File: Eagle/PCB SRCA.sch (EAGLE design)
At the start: 59 parts, among them IC1 DSPIC30F4011-30I_P, IC2 LM324LVIDR, IC3 LMT86QDCKRQ1, IC4 TXB0108PWR, IC5 LORA_MOTE, J1 TBL002A-350-03GR-2OR, J2 TBL002A-350-03GR-2OR, J3 TBL002A-350-03GR-2OR, J4 172447-0004, Q1 TIP41C, T1 2N3904, T10 2N3904, T11 2N3904, T2 2N3904, T3 2N3904, T4 2N3904, T5 2N3904, T6 2N3904, T7 2N3904, T8 2N3904, T9 2N3904

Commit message: 14/07/2021
actualizacIón de la PCB
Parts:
- removed C4: C0805X104K1RAC3316, C0805X104K1RAC3316:C0805X104K1RAC3316
- removed IC5: LORA_MOTE, LORA_MOTE:LORA_MOTE
- removed R17: ERA6AEB101V, ERA6AEB101V:ERA6AEB101V
- IC4: value TXB0108PWR -> LORA_MOTE; device TXB0108PWR:TXB0108PWR -> LORA_MOTE:LORA_MOTE
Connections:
- removed net FAN2: D1.A, J2.B1, Q1.C
- removed net GND2: T11.E
- removed net N$20: IC4.OE, R17.2
- removed net V1: R18.2
- removed net V3: IC4.VCCA
- new net I2C_SCL: IC1.PGD/EMUD/U1TX/SDO1/SCL/RF3, J3.A2
- new net I2C_SDA: IC1.PGC/EMUC/U1RX/SDI1/SDA/RF2, J3.B1
- new net TX_UART2: IC1.U2TX/CN18/RF5
- net FAN1: now also D1.A, J2.B1, Q1.C; no longer D1.C, J2.A2
- net GND: no longer C4.1, IC5.GND, R17.1
- net GND1: now also T11.E
- net RX_LORA: now also IC4.UARTTX; no longer IC4.A1, IC5.UARTTX
- net RX_UART: no longer IC4.B1
- net SONAR_ADC: now also J2.A2; no longer J2.A1
- net TX_LORA: now also IC4.UARTRX; no longer IC4.A2, IC5.UARTRX
- net TX_UART: no longer IC4.B2
- net V5: now also D1.C, IC4.V5, J2.A1, R18.2; no longer C4.2, IC4.VCCB, IC5.V5

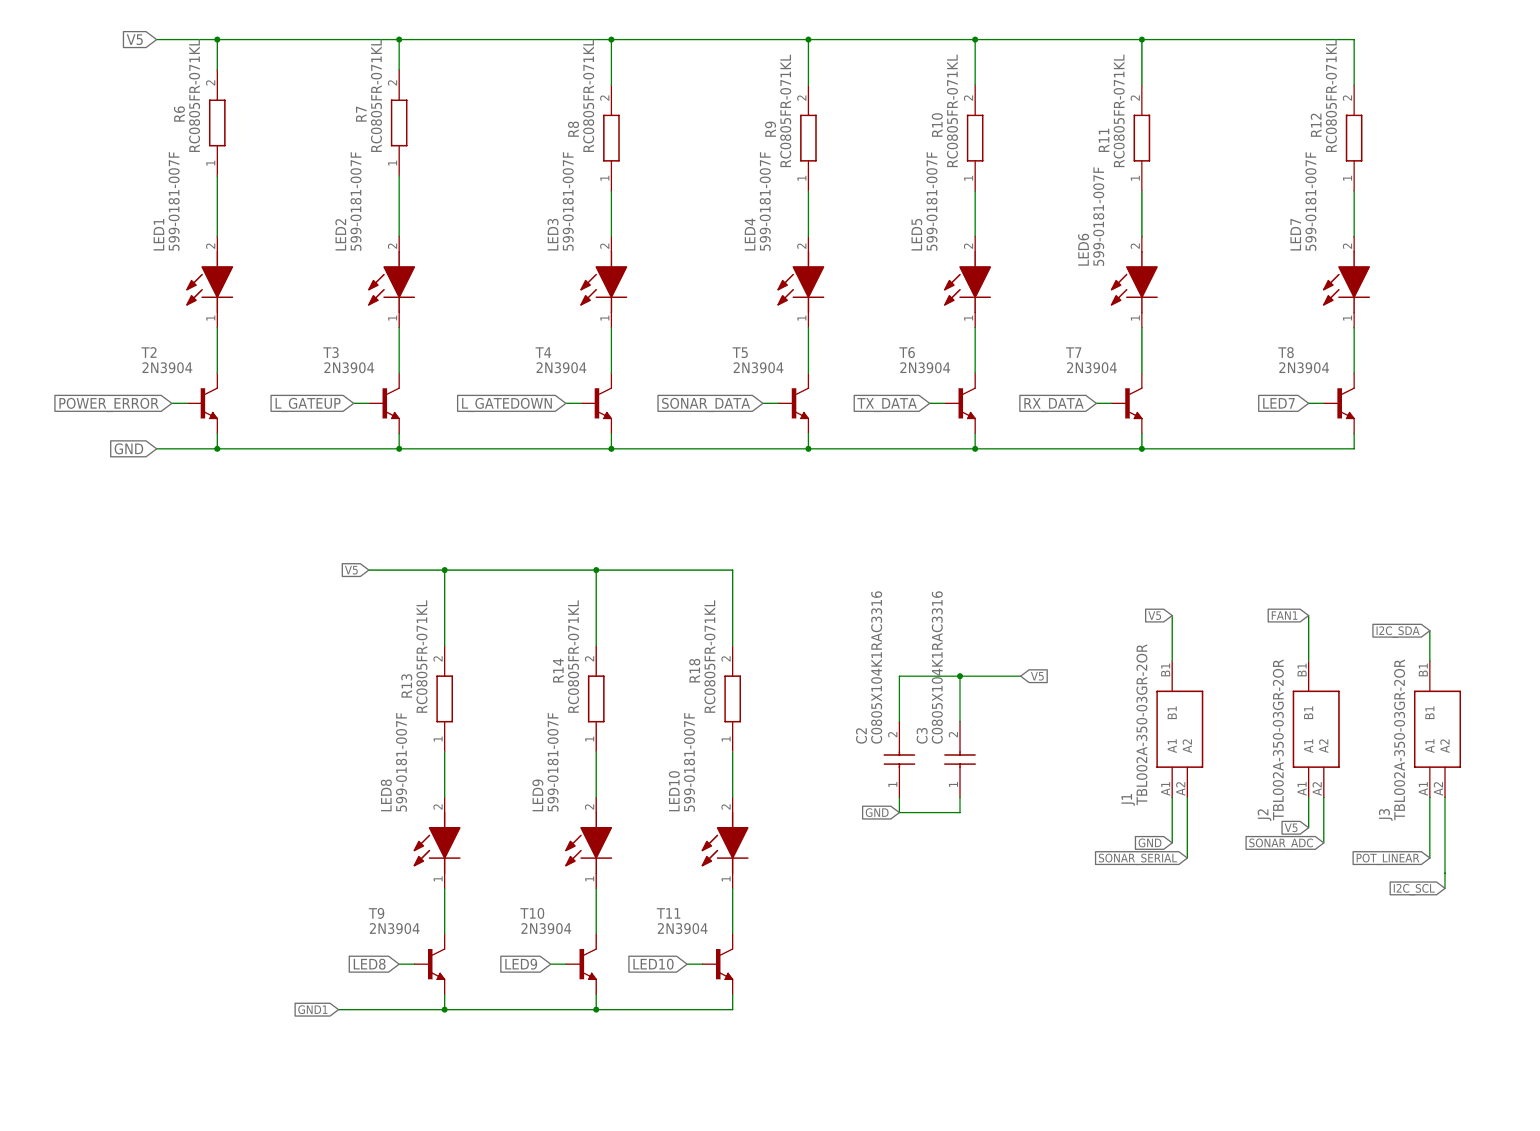
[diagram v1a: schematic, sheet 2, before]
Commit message: 21/07/2021
cambios en las posiciones de los componentes y pistas
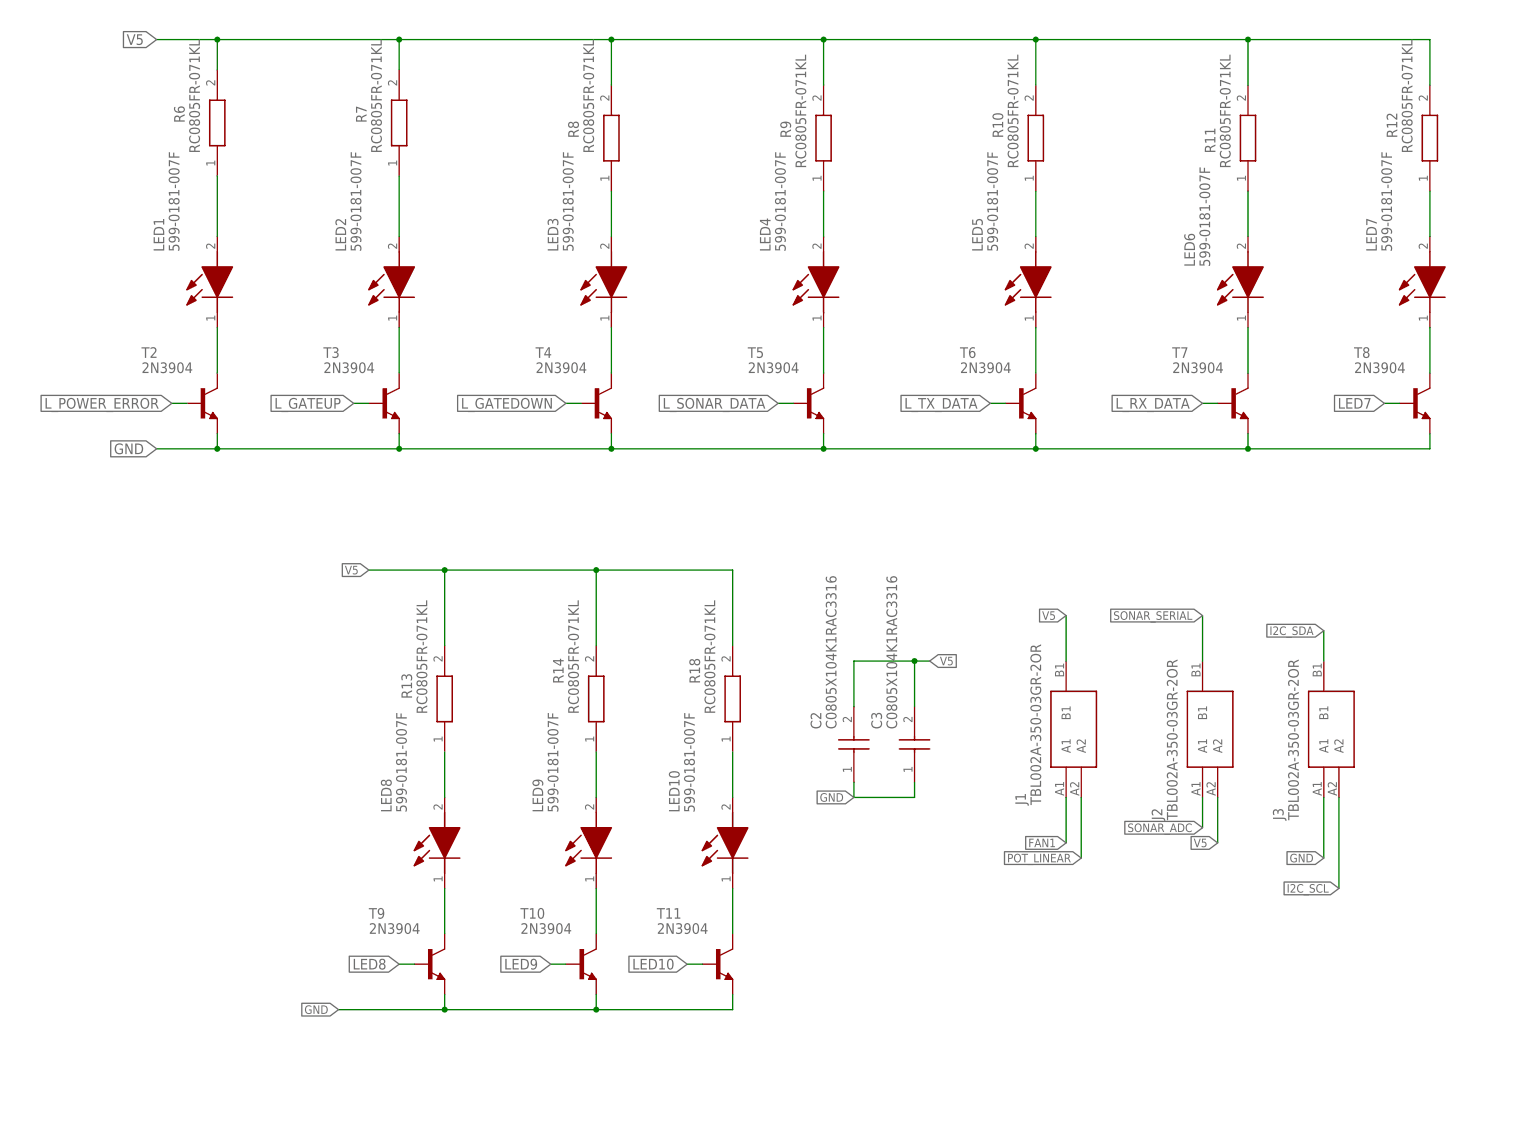
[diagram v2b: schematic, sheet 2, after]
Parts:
- added J5: ICSP, ICSP:ICSP
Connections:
- net POWER_ERROR renamed L_POWER_ERROR
- net RX_DATA renamed L_RX_DATA
- net SONAR_DATA renamed L_SONAR_DATA
- net TX_DATA renamed L_TX_DATA
- removed net GND1: T10.E, T11.E, T9.E
- new net N$20: S3.NO_1
- net FAN1: now also J1.A1; no longer J2.B1
- net GATE_DOWN: now also IC1.EMUC2/OC1/IC1/INT1/RD0; no longer IC1.OC4/RD3
- net GATE_UP: now also IC1.SCK1/RF6; no longer IC1.EMUD2/OC2/IC2/INT2/RD1
- net GND: now also J3.A1, J5.VSS, T10.E, T11.E, T9.E; no longer J1.A1
- net I2C_SCL: now also J5.PGD
- net I2C_SDA: now also J5.PGC
- net LED10: now also IC1.OC4/RD3; no longer IC1.!FLTA!/INT0/RE8
- net LED8: now also IC1.!FLTA!/INT0/RE8; no longer IC1.EMUD1/SOSCI/T2CK/U1ATX/CN1/RC13
- net LED9: now also IC1.EMUD2/OC2/IC2/INT2/RD1; no longer IC1.EMUC1/SOSCO/T1CK/U1ARX/CN0/RC14
- net MCLR: now also J5.MCLR
- net POT_LINEAR: now also J1.A2; no longer J3.A1
- net RX_UART: now also IC1.EMUC1/SOSCO/T1CK/U1ARX/CN0/RC14; no longer IC1.C1RX/RF0
- net SONAR_ADC: now also J2.A1; no longer J2.A2
- net SONAR_SERIAL: now also J2.B1; no longer J1.A2
- net TX_UART: now also IC1.EMUD1/SOSCI/T2CK/U1ATX/CN1/RC13; no longer IC1.C1TX/RF1
- net V5: now also J2.A2, J5.VDD, S3.NO_2; no longer J2.A1, S3.NO_1
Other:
- moved on the sheet: C2, C3, J1, J2, J3, LED4, LED5, LED6, LED7, R10, R11, R12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

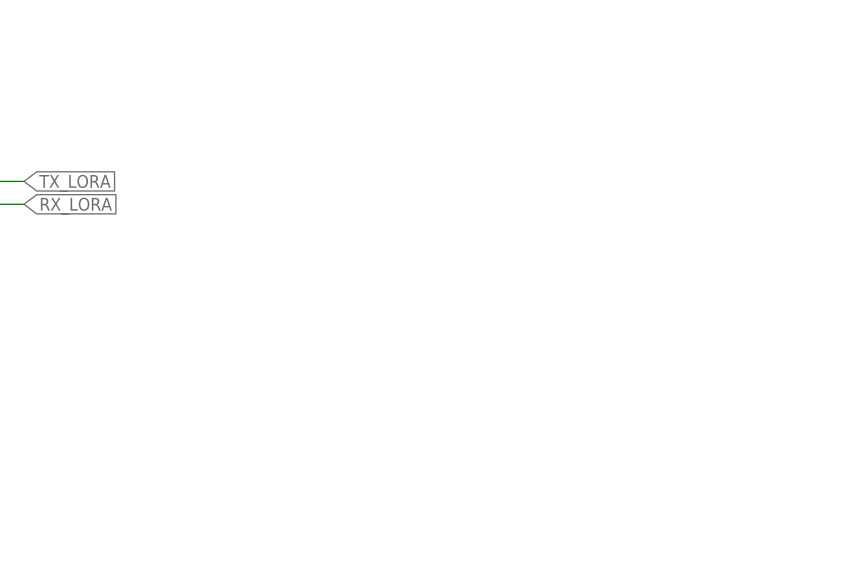
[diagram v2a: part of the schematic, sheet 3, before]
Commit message: 22/07/2021
Se actualizo la pcb con todos los componentes y pistas, además se agregó las librerías del proyecto
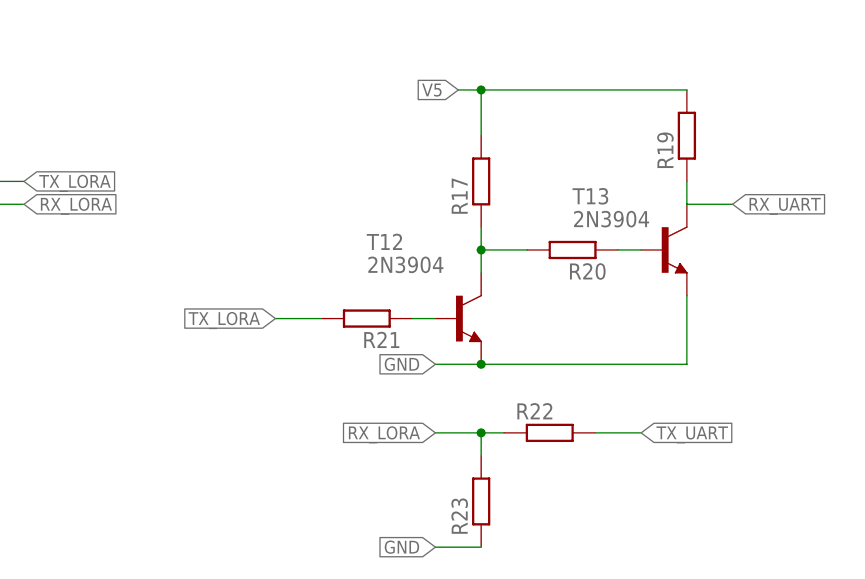
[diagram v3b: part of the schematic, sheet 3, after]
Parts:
- added R17, R19, R20, R21, R22, R23: (no value), rcl:R-EU_0207/10
- added T12, T13: 2N3904, transistor-neu-to92:2N3904
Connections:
- new net N$23: R17.1, R20.2, T12.C
- new net N$24: R21.1, T12.B
- new net N$26: R20.1, T13.B
- net GND: now also R23.1, T12.E, T13.E
- net RX_LORA: now also R22.1, R23.2
- net RX_UART: now also R19.1, T13.C
- net TX_LORA: now also R21.2
- net TX_UART: now also R22.2
- net V5: now also R17.2, R19.2
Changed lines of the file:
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@@
 <part name="R5" library="RC0805FR-071KL" deviceset="RC0805FR-071KL" device=""/>
 <part name="R2" library="ERA-6VEB1002V" deviceset="ERA-6VEB1002V" device=""/>
+<part name="T12" library="transistor-neu-to92" library_urn="urn:adsk.eagle:library:397" deviceset="2N3904" device="" package3d_urn="urn:adsk.eagle:package:28725/2"/>
+<part name="T13" library="transistor-neu-to92" library_urn="urn:adsk.eagle:library:397" deviceset="2N3904" device="" package3d_urn="urn:adsk.eagle:package:28725/2"/>
+<part name="R17" library="rcl" library_urn="urn:adsk.eagle:library:334" deviceset="R-EU_" device="0207/10" package3d_urn="urn:adsk.eagle:package:23491/2"/>
+<part name="R19" library="rcl" library_urn="urn:adsk.eagle:library:334" deviceset="R-EU_" device="0207/10" package3d_urn="urn:adsk.eagle:package:23491/2"/>
+<part name="R20" library="rcl" library_urn="urn:adsk.eagle:library:334" deviceset="R-EU_" device="0207/10" package3d_urn="urn:adsk.eagle:package:23491/2"/>
+<part name="R21" library="rcl" library_urn="urn:adsk.eagle:library:334" deviceset="R-EU_" device="0207/10" package3d_urn="urn:adsk.eagle:package:23491/2"/>
+<part name="R22" library="rcl" library_urn="urn:adsk.eagle:library:334" deviceset="R-EU_" device="0207/10" package3d_urn="urn:adsk.eagle:package:23491/2"/>
+<part name="R23" library="rcl" library_urn="urn:adsk.eagle:library:334" deviceset="R-EU_" device="0207/10" package3d_urn="urn:adsk.eagle:package:23491/2"/>
 </parts>
 <sheets>
@@
 <attribute name="VALUE" x="22.86" y="124.46" size="1.778" layer="96"/>
 </instance>
+<instance part="T12" gate="G1" x="114.3" y="149.86" smashed="yes">
+<attribute name="NAME" x="104.14" y="157.48" size="1.778" layer="95"/>
+<attribute name="VALUE" x="104.14" y="154.94" size="1.778" layer="96"/>
+</instance>
+<instance part="T13" gate="G1" x="137.16" y="157.48" smashed="yes">
+<attribute name="NAME" x="127" y="162.56" size="1.778" layer="95"/>
+<attribute name="VALUE" x="127" y="160.02" size="1.778" layer="96"/>
+</instance>
+<instance part="R17" gate="G$1" x="116.84" y="165.1" smashed="yes" rot="R90">
+<attribute name="NAME" x="115.3414" y="161.29" size="1.778" layer="95" rot="R90"/>
+<attribute name="VALUE" x="120.142" y="161.29" size="1.778" layer="96" rot="R90"/>
+</instance>
+<instance part="R19" gate="G$1" x="139.7" y="170.18" smashed="yes" rot="R90">
+<attribute name="NAME" x="138.2014" y="166.37" size="1.778" layer="95" rot="R90"/>
+<attribute name="VALUE" x="143.002" y="166.37" size="1.778" layer="96" rot="R90"/>
+</instance>
+<instance part="R20" gate="G$1" x="127" y="157.48" smashed="yes" rot="R180">
+<attribute name="NAME" x="130.81" y="155.9814" size="1.778" layer="95" rot="R180"/>
+<attribute name="VALUE" x="130.81" y="160.782" size="1.778" layer="96" rot="R180"/>
+</instance>
+<instance part="R21" gate="G$1" x="104.14" y="149.86" smashed="yes" rot="R180">
+<attribute name="NAME" x="107.95" y="148.3614" size="1.778" layer="95" rot="R180"/>
+<attribute name="VALUE" x="107.95" y="153.162" size="1.778" layer="96" rot="R180"/>
+</instance>
+<instance part="R22" gate="G$1" x="124.46" y="137.16" smashed="yes">
+<attribute name="NAME" x="120.65" y="138.6586" size="1.778" layer="95"/>
+<attribute name="VALUE" x="120.65" y="133.858" size="1.778" layer="96"/>
+</instance>
+<instance part="R23" gate="G$1" x="116.84" y="129.54" smashed="yes" rot="R90">
+<attribute name="NAME" x="115.3414" y="125.73" size="1.778" layer="95" rot="R90"/>
+<attribute name="VALUE" x="120.142" y="125.73" size="1.778" layer="96" rot="R90"/>
+</instance>
 </instances>
 <busses>
@@
 <pinref part="IC4" gate="G$1" pin="V5"/>
 </segment>
+<segment>
+<pinref part="R19" gate="G$1" pin="2"/>
+<pinref part="R17" gate="G$1" pin="2"/>
+<wire x1="139.7" y1="175.26" x2="116.84" y2="175.26" width="0.1524" layer="91"/>
+<wire x1="116.84" y1="175.26" x2="116.84" y2="170.18" width="0.1524" layer="91"/>
+<wire x1="116.84" y1="175.26" x2="114.3" y2="175.26" width="0.1524" layer="91"/>
+<junction x="116.84" y="175.26"/>
+<label x="114.3" y="175.26" size="1.4224" layer="95" rot="R180" xref="yes"/>
+</segment>
 </net>
 <net name="GND" class="0">
@@
 <pinref part="IC4" gate="G$1" pin="GND"/>
 </segment>
+<segment>
+<pinref part="T12" gate="G1" pin="E"/>
+<pinref part="T13" gate="G1" pin="E"/>
+<wire x1="116.84" y1="144.78" x2="139.7" y2="144.78" width="0.1524" layer="91"/>
+<wire x1="139.7" y1="144.78" x2="139.7" y2="152.4" width="0.1524" layer="91"/>
+<wire x1="116.84" y1="144.78" x2="111.76" y2="144.78" width="0.1524" layer="91"/>
+<junction x="116.84" y="144.78"/>
+<label x="111.76" y="144.78" size="1.4224" layer="95" rot="R180" xref="yes"/>
+</segment>
+<segment>
+<pinref part="R23" gate="G$1" pin="1"/>
+<wire x1="116.84" y1="124.46" x2="111.76" y2="124.46" width="0.1524" layer="91"/>
+<label x="111.76" y="124.46" size="1.4224" layer="95" rot="R180" xref="yes"/>
+</segment>
 </net>
 <net name="TX_LORA" class="0">
@@
 <pinref part="IC4" gate="G$1" pin="UARTRX"/>
 </segment>
+<segment>
+<pinref part="R21" gate="G$1" pin="2"/>
+<wire x1="99.06" y1="149.86" x2="93.98" y2="149.86" width="0.1524" layer="91"/>
+<label x="93.98" y="149.86" size="1.4224" layer="95" rot="R180" xref="yes"/>
+</segment>
 </net>
 <net name="RX_LORA" class="0">
@@
 <pinref part="IC4" gate="G$1" pin="UARTTX"/>
 </segment>
-</net>
+<segment>
+<pinref part="R22" gate="G$1" pin="1"/>
+<pinref part="R23" gate="G$1" pin="2"/>
+<wire x1="119.38" y1="137.16" x2="116.84" y2="137.16" width="0.1524" layer="91"/>
+<wire x1="116.84" y1="137.16" x2="116.84" y2="134.62" width="0.1524" layer="91"/>
+<wire x1="116.84" y1="137.16" x2="111.76" y2="137.16" width="0.1524" layer="91"/>
+<junction x="116.84" y="137.16"/>
+<label x="111.76" y="137.16" size="1.4224" layer="95" rot="R180" xref="yes"/>
+</segment>
+</net>
+<net name="N$23" class="0">
+<segment>
+<pinref part="R17" gate="G$1" pin="1"/>
+<pinref part="T12" gate="G1" pin="C"/>
+<wire x1="116.84" y1="160.02" x2="116.84" y2="157.48" width="0.1524" layer="91"/>
+<pinref part="R20" gate="G$1" pin="2"/>
+<wire x1="116.84" y1="157.48" x2="116.84" y2="154.94" width="0.1524" layer="91"/>
+<wire x1="121.92" y1="157.48" x2="116.84" y2="157.48" width="0.1524" layer="91"/>
+<junction x="116.84" y="157.48"/>
+</segment>
+</net>
+<net name="N$24" class="0">
+<segment>
+<pinref part="R21" gate="G$1" pin="1"/>
+<pinref part="T12" gate="G1" pin="B"/>
+<wire x1="109.22" y1="149.86" x2="111.76" y2="149.86" width="0.1524" layer="91"/>
+</segment>
+</net>
+<net name="N$26" class="0">
+<segment>
+<pinref part="R20" gate="G$1" pin="1"/>
+<pinref part="T13" gate="G1" pin="B"/>
+<wire x1="132.08" y1="157.48" x2="134.62" y2="157.48" width="0.1524" layer="91"/>
+</segment>
+</net>
+<net name="RX_UART" class="0">
+<segment>
+<pinref part="T13" gate="G1" pin="C"/>
+<pinref part="R19" gate="G$1" pin="1"/>
+<wire x1="139.7" y1="165.1" x2="139.7" y2="162.56" width="0.1524" layer="91"/>
+<wire x1="139.7" y1="162.56" x2="144.78" y2="162.56" width="0.1524" layer="91"/>
+<label x="144.78" y="162.56" size="1.4224" layer="95" xref="yes"/>
+</segment>
+</net>
+<net name="TX_UART" class="0">
+<segment>
+<pinref part="R22" gate="G$1" pin="2"/>
+<wire x1="129.54" y1="137.16" x2="134.62" y2="137.16" width="0.1524" layer="91"/>
+<label x="134.62" y="137.16" size="1.4224" layer="95" xref="yes"/>
+</segment>
+</net>
